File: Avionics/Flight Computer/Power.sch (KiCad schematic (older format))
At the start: 17 parts, among them U8 MAX17243

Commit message: Changed LED configuration, added smart driver chip to let all the CPUs access it..
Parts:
- C45, C47, R10, R11, R13: Voltage 50V -> 16V
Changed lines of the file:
@@
 BIAS
 $Comp
-L GND #PWR0119
+L GND #PWR0123
 U 1 1 58AB8EE1
 P 6050 4450
-F 0 "#PWR0119" H 2800 -350 50  0001 C CNN
+F 0 "#PWR0123" H 2800 -350 50  0001 C CNN
 F 1 "GND" H 6055 4277 50  0000 C CNN
 F 2 "" H 2800 -100 50  0001 C CNN
@@
 R11 sets oscillation frequency to 2.2MHz
 $Comp
-L +3.3V #PWR0120
+L +3.3V #PWR0124
 U 1 1 58AB9BA4
 P 8600 3100
-F 0 "#PWR0120" H 3600 0   50  0001 C CNN
+F 0 "#PWR0124" H 3600 0   50  0001 C CNN
 F 1 "+3.3V" H 8615 3273 50  0000 C CNN
 F 2 "" H 3600 150 50  0001 C CNN
@@
 PGOOD
 $Comp
-L GND #PWR0121
+L GND #PWR0125
 U 1 1 58ABCF35
 P 3500 3300
-F 0 "#PWR0121" H 250 -1500 50  0001 C CNN
+F 0 "#PWR0125" H 250 -1500 50  0001 C CNN
 F 1 "GND" H 3505 3127 50  0000 C CNN
 F 2 "" H 250 -1250 50  0001 C CNN
@@
 $EndComp
 $Comp
-L GND #PWR0122
+L GND #PWR0126
 U 1 1 58ABD05E
 P 2750 3300
-F 0 "#PWR0122" H -500 -1500 50  0001 C CNN
+F 0 "#PWR0126" H -500 -1500 50  0001 C CNN
 F 1 "GND" H 2755 3127 50  0000 C CNN
 F 2 "" H -500 -1250 50  0001 C CNN
@@
 Connection ~ 2750 2900
 $Comp
-L GND #PWR0123
+L GND #PWR0127
 U 1 1 58ABDCB9
 P 2000 3300
-F 0 "#PWR0123" H -1250 -1500 50  0001 C CNN
+F 0 "#PWR0127" H -1250 -1500 50  0001 C CNN
 F 1 "GND" H 2005 3127 50  0000 C CNN
 F 2 "" H -1250 -1250 50  0001 C CNN
@@
 Connection ~ 8250 3100
 $Comp
-L GND #PWR0124
+L GND #PWR0128
 U 1 1 58ABEDD8
 P 7850 3450
-F 0 "#PWR0124" H 4600 -1350 50  0001 C CNN
+F 0 "#PWR0128" H 4600 -1350 50  0001 C CNN
 F 1 "GND" H 7855 3277 50  0000 C CNN
 F 2 "" H 4600 -1100 50  0001 C CNN
@@
 $EndComp
 $Comp
-L GND #PWR0125
+L GND #PWR0129
 U 1 1 58ABEEB5
 P 8250 3450
-F 0 "#PWR0125" H 5000 -1350 50  0001 C CNN
+F 0 "#PWR0129" H 5000 -1350 50  0001 C CNN
 F 1 "GND" H 8255 3277 50  0000 C CNN
 F 2 "" H 5000 -1100 50  0001 C CNN
@@
 	850  2450 850  2350
 $Comp
-L +BATT #PWR0126
+L +BATT #PWR0130
 U 1 1 58B2E558
 P 850 2850
-F 0 "#PWR0126" H -200 -50 50  0001 C CNN
+F 0 "#PWR0130" H -200 -50 50  0001 C CNN
 F 1 "+BATT" H 865 3023 50  0000 C CNN
 F 2 "" H -200 100 50  0001 C CNN
@@
 $EndComp
 $Comp
-L VUSB #PWR0127
+L VUSB #PWR0131
 U 1 1 58B2E98C
 P 850 2350
-F 0 "#PWR0127" H -300 250 50  0001 C CNN
+F 0 "#PWR0131" H -300 250 50  0001 C CNN
 F 1 "VUSB" H 865 2523 50  0000 C CNN
 F 2 "" H -300 400 50  0001 C CNN
@@
 F 3 "" V -370 1100 50  0001 C CNN
 F 4 "1%" H 4220 3659 60  0000 L CNN "Tolerance"
-F 5 "50V" V -200 1100 60  0001 C CNN "Voltage"
+F 5 "16V" V -200 1100 60  0001 C CNN "Voltage"
 F 6 "0.062W" V -100 1100 60  0001 C CNN "Power"
 F 7 "Thin Film" V 0   1100 60  0001 C CNN "Material"
@@
 F 2 "Capacitors_SMD:C_0402" H 2288 -300 50  0001 C CNN
 F 3 "" H 2250 -150 50  0001 C CNN
-F 4 "50V" H 2350 -200 60  0001 L CNN "Voltage"
+F 4 "16V" H 2350 -200 60  0001 L CNN "Voltage"
 F 5 "20%" H 2350 -100 60  0001 L CNN "Tolerance"
 F 6 "X7R" H 2300 0   60  0001 L CNN "Type"
@@
 F 3 "" V 30  1450 50  0001 C CNN
 F 4 "1%" H 4620 4009 60  0000 L CNN "Tolerance"
-F 5 "50V" V 200 1450 60  0001 C CNN "Voltage"
+F 5 "16V" V 200 1450 60  0001 C CNN "Voltage"
 F 6 "0.062W" V 300 1450 60  0001 C CNN "Power"
 F 7 "Thin Film" V 400 1450 60  0001 C CNN "Material"
@@
 F 2 "Capacitors_SMD:C_0402" H 4888 -1050 50  0001 C CNN
 F 3 "" H 4850 -900 50  0001 C CNN
-F 4 "50V" H 4950 -950 60  0001 L CNN "Voltage"
+F 4 "16V" H 4950 -950 60  0001 L CNN "Voltage"
 F 5 "20%" H 4950 -850 60  0001 L CNN "Tolerance"
 F 6 "X7R" H 4900 -750 60  0001 L CNN "Type"
@@
 F 3 "" V 2930 750 50  0001 C CNN
 F 4 "1%" H 7520 3309 60  0000 L CNN "Tolerance"
-F 5 "50V" V 3100 750 60  0001 C CNN "Voltage"
+F 5 "16V" V 3100 750 60  0001 C CNN "Voltage"
 F 6 "0.062W" V 3200 750 60  0001 C CNN "Power"
 F 7 "Thin Film" V 3300 750 60  0001 C CNN "Material"
@@
 $EndComp
 $Comp
-L PWR_FLAG #FLG0128
+L PWR_FLAG #FLG0132
 U 1 1 58BE5ADD
 P 8150 3100
-F 0 "#FLG0128" H 8200 3150 50  0001 C CNN
+F 0 "#FLG0132" H 8200 3150 50  0001 C CNN
 F 1 "PWR_FLAG" H 8150 3274 50  0000 C CNN
 F 2 "" H -1500 550 50  0001 C CNN
@@
 Connection ~ 8150 3100
 $Comp
-L PWR_FLAG #FLG0129
+L PWR_FLAG #FLG0133
 U 1 1 58BE6F80
 P 4300 2900
-F 0 "#FLG0129" H 0   925 50  0001 C CNN
+F 0 "#FLG0133" H 0   925 50  0001 C CNN
 F 1 "PWR_FLAG" H 4300 3074 50  0000 C CNN
 F 2 "" H 0   850 50  0001 C CNN

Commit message: DFM/BOM Optimizations
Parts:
- R10: value 20k -> 18k
- R11: value 12k -> 15k
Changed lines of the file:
@@
 P 4150 3750
 F 0 "R10" H 4220 3849 50  0000 L CNN
-F 1 "20k" H 4220 3758 50  0000 L CNN
+F 1 "18k" H 4220 3758 50  0000 L CNN
 F 2 "Resistors_SMD:R_0402" V -650 1100 50  0001 C CNN
 F 3 "" V -370 1100 50  0001 C CNN
@@
 P 4550 4100
 F 0 "R11" H 4620 4199 50  0000 L CNN
-F 1 "12k" H 4620 4108 50  0000 L CNN
+F 1 "15k" H 4620 4108 50  0000 L CNN
 F 2 "Resistors_SMD:R_0402" V -250 1450 50  0001 C CNN
 F 3 "" V 30  1450 50  0001 C CNN

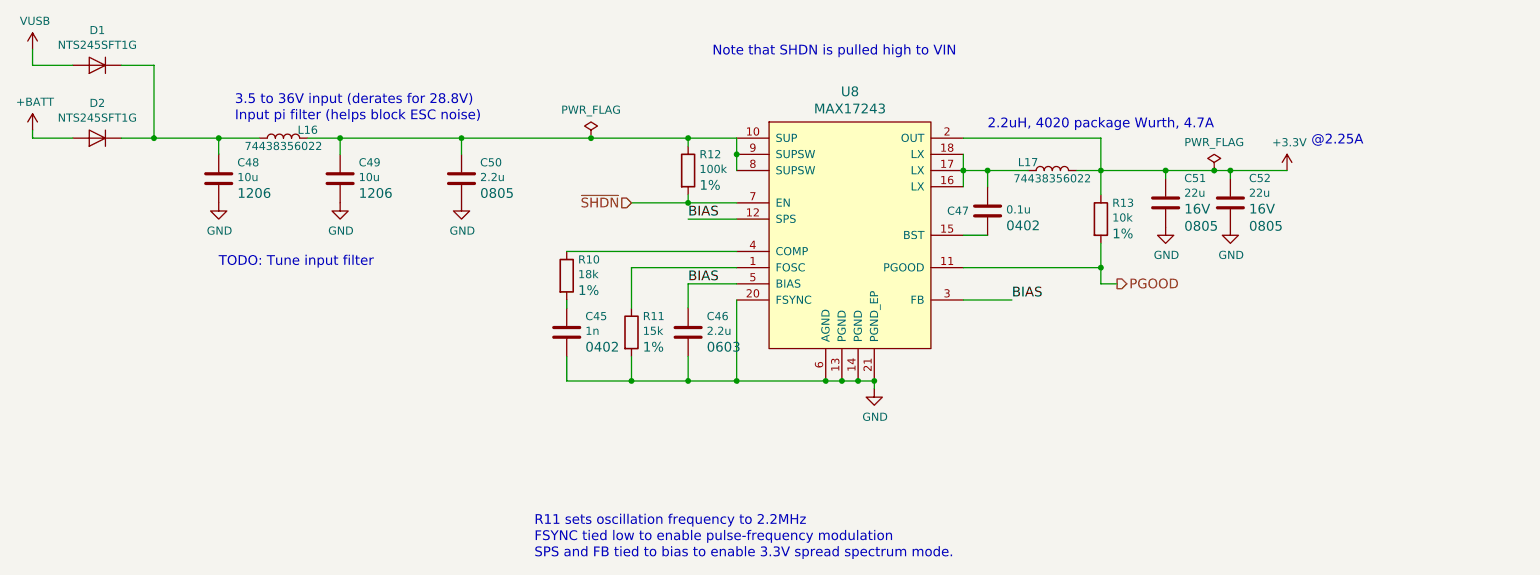
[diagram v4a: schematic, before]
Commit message: Built outputs and added manufacturing part numbers to make BOM search easier.
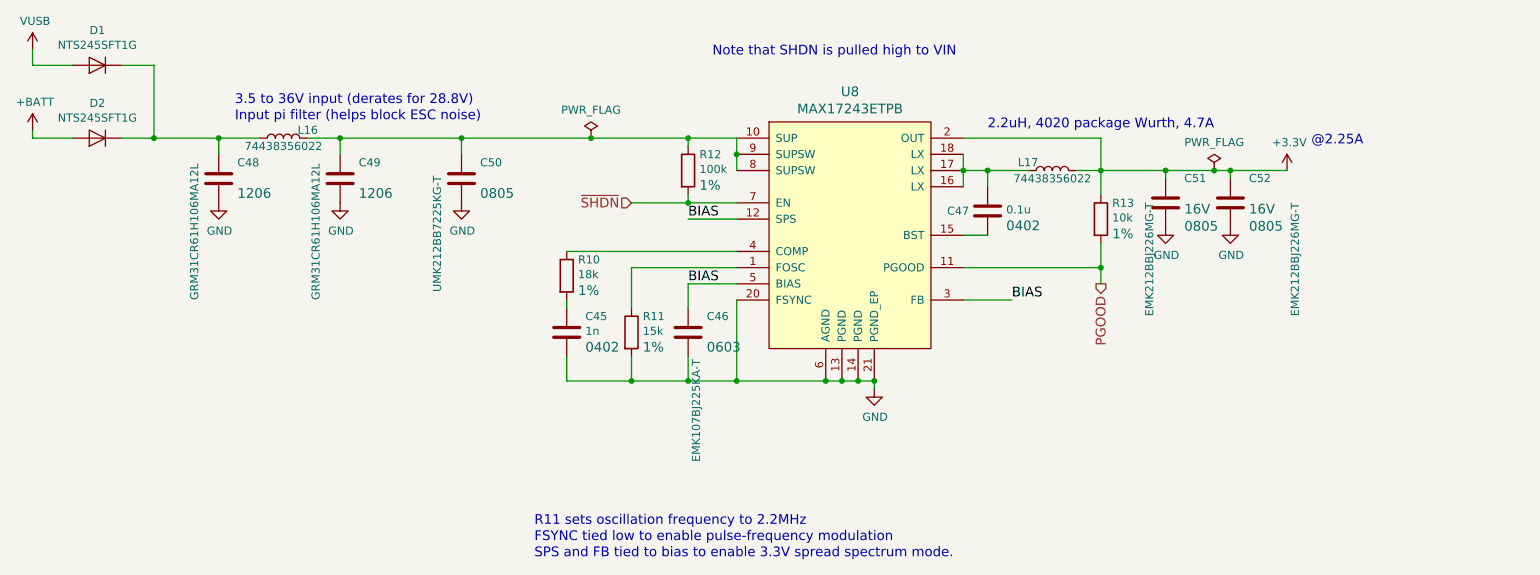
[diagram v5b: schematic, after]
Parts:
- C46: value 2.2u -> EMK107BJ225KA-T
- C48, C49: value 10u -> GRM31CR61H106MA12L
- C50: value 2.2u -> UMK212BB7225KG-T
- C51, C52: value 22u -> EMK212BBJ226MG-T
- U8: value MAX17243 -> MAX17243ETPB
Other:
- note removed: "TODO: Tune input filter"
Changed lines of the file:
@@
 BIAS
 $Comp
-L GND #PWR114
+L GND #PWR0123
 U 1 1 58AB8EE1
 P 6050 4450
-F 0 "#PWR114" H 2800 -350 50  0001 C CNN
+F 0 "#PWR0123" H 2800 -350 50  0001 C CNN
 F 1 "GND" H 6055 4277 50  0000 C CNN
 F 2 "" H 2800 -100 50  0001 C CNN
@@
 R11 sets oscillation frequency to 2.2MHz
 $Comp
-L +3.3V #PWR117
+L +3.3V #PWR0124
 U 1 1 58AB9BA4
 P 8600 3100
-F 0 "#PWR117" H 3600 0   50  0001 C CNN
+F 0 "#PWR0124" H 3600 0   50  0001 C CNN
 F 1 "+3.3V" H 8615 3273 50  0000 C CNN
 F 2 "" H 3600 150 50  0001 C CNN
@@
 Text HLabel 4550 3300 0    60   Input ~ 0
 ~SHDN
-Text HLabel 7550 3800 2    60   Output ~ 0
+Text HLabel 7450 3800 3    60   Output ~ 0
 PGOOD
 $Comp
-L GND #PWR113
+L GND #PWR0125
 U 1 1 58ABCF35
 P 3500 3300
-F 0 "#PWR113" H 250 -1500 50  0001 C CNN
+F 0 "#PWR0125" H 250 -1500 50  0001 C CNN
 F 1 "GND" H 3505 3127 50  0000 C CNN
 F 2 "" H 250 -1250 50  0001 C CNN
@@
 $EndComp
 $Comp
-L GND #PWR112
+L GND #PWR0126
 U 1 1 58ABD05E
 P 2750 3300
-F 0 "#PWR112" H -500 -1500 50  0001 C CNN
+F 0 "#PWR0126" H -500 -1500 50  0001 C CNN
 F 1 "GND" H 2755 3127 50  0000 C CNN
 F 2 "" H -500 -1250 50  0001 C CNN
@@
 Connection ~ 2750 2900
 $Comp
-L GND #PWR111
+L GND #PWR0127
 U 1 1 58ABDCB9
 P 2000 3300
-F 0 "#PWR111" H -1250 -1500 50  0001 C CNN
+F 0 "#PWR0127" H -1250 -1500 50  0001 C CNN
 F 1 "GND" H 2005 3127 50  0000 C CNN
 F 2 "" H -1250 -1250 50  0001 C CNN
@@
 Connection ~ 8250 3100
 $Comp
-L GND #PWR115
+L GND #PWR0128
 U 1 1 58ABEDD8
 P 7850 3450
-F 0 "#PWR115" H 4600 -1350 50  0001 C CNN
+F 0 "#PWR0128" H 4600 -1350 50  0001 C CNN
 F 1 "GND" H 7855 3277 50  0000 C CNN
 F 2 "" H 4600 -1100 50  0001 C CNN
@@
 $EndComp
 $Comp
-L GND #PWR116
+L GND #PWR0129
 U 1 1 58ABEEB5
 P 8250 3450
-F 0 "#PWR116" H 5000 -1350 50  0001 C CNN
+F 0 "#PWR0129" H 5000 -1350 50  0001 C CNN
 F 1 "GND" H 8255 3277 50  0000 C CNN
 F 2 "" H 5000 -1100 50  0001 C CNN
@@
 	0    -1   -1   0
 $EndComp
-Text Notes 2000 3700 0    60   ~ 0
-TODO: Tune input filter
-Wire Wire Line
-	7450 3800 7550 3800
 Wire Wire Line
 	7450 3700 6600 3700
@@
 	850  2450 850  2350
 $Comp
-L +BATT #PWR110
+L +BATT #PWR0130
 U 1 1 58B2E558
 P 850 2850
-F 0 "#PWR110" H -200 -50 50  0001 C CNN
+F 0 "#PWR0130" H -200 -50 50  0001 C CNN
 F 1 "+BATT" H 865 3023 50  0000 C CNN
 F 2 "" H -200 100 50  0001 C CNN
@@
 $EndComp
 $Comp
-L VUSB #PWR109
+L VUSB #PWR0131
 U 1 1 58B2E98C
 P 850 2350
-F 0 "#PWR109" H -300 250 50  0001 C CNN
+F 0 "#PWR0131" H -300 250 50  0001 C CNN
 F 1 "VUSB" H 865 2523 50  0000 C CNN
 F 2 "" H -300 400 50  0001 C CNN
@@
 P 2000 3150
 F 0 "C48" H 2115 3249 50  0000 L CNN
-F 1 "10u" H 2115 3158 50  0000 L CNN
+F 1 "GRM31CR61H106MA12L" V 1850 2400 50  0000 L CNN
 F 2 "Capacitors_SMD:C_1206" H 138 -1250 50  0001 C CNN
 F 3 "" H 100 -1100 50  0001 C CNN
@@
 P 2750 3150
 F 0 "C49" H 2865 3249 50  0000 L CNN
-F 1 "10u" H 2865 3158 50  0000 L CNN
+F 1 "GRM31CR61H106MA12L" V 2600 2400 50  0000 L CNN
 F 2 "Capacitors_SMD:C_1206" H 888 -1250 50  0001 C CNN
 F 3 "" H 850 -1100 50  0001 C CNN
@@
 P 3500 3150
 F 0 "C50" H 3615 3249 50  0000 L CNN
-F 1 "2.2u" H 3615 3158 50  0000 L CNN
+F 1 "UMK212BB7225KG-T" V 3350 2450 50  0000 L CNN
 F 2 "Capacitors_SMD:C_0805" H 1638 -1250 50  0001 C CNN
 F 3 "" H 1600 -1100 50  0001 C CNN
@@
 P 4900 4100
 F 0 "C46" H 5015 4199 50  0000 L CNN
-F 1 "2.2u" H 5015 4108 50  0000 L CNN
+F 1 "EMK107BJ225KA-T" V 4950 3300 50  0000 L CNN
 F 2 "Capacitors_SMD:C_0603" H 3038 -300 50  0001 C CNN
 F 3 "" H 3000 -150 50  0001 C CNN
@@
 P 7850 3300
 F 0 "C51" H 7965 3452 50  0000 L CNN
-F 1 "22u" H 7965 3361 50  0000 L CNN
+F 1 "EMK212BBJ226MG-T" V 7750 2600 50  0000 L CNN
 F 2 "Capacitors_SMD:C_0805" H 5988 -1100 50  0001 C CNN
 F 3 "" H 5950 -950 50  0001 C CNN
@@
 P 8250 3300
 F 0 "C52" H 8365 3452 50  0000 L CNN
-F 1 "22u" H 8365 3361 50  0000 L CNN
+F 1 "EMK212BBJ226MG-T" V 8650 2600 50  0000 L CNN
 F 2 "Capacitors_SMD:C_0805" H 6388 -1100 50  0001 C CNN
 F 3 "" H 6350 -950 50  0001 C CNN
@@
 $EndComp
 $Comp
-L PWR_FLAG #FLG16
+L PWR_FLAG #FLG0132
 U 1 1 58BE5ADD
 P 8150 3100
-F 0 "#FLG16" H 8200 3150 50  0001 C CNN
+F 0 "#FLG0132" H 8200 3150 50  0001 C CNN
 F 1 "PWR_FLAG" H 8150 3274 50  0000 C CNN
 F 2 "" H -1500 550 50  0001 C CNN
@@
 Connection ~ 8150 3100
 $Comp
-L PWR_FLAG #FLG15
+L PWR_FLAG #FLG0133
 U 1 1 58BE6F80
 P 4300 2900
-F 0 "#FLG15" H 0   925 50  0001 C CNN
+F 0 "#FLG0133" H 0   925 50  0001 C CNN
 F 1 "PWR_FLAG" H 4300 3074 50  0000 C CNN
 F 2 "" H 0   850 50  0001 C CNN
@@
 P 5900 3500
 F 0 "U8" H 5900 4387 60  0000 C CNN
-F 1 "MAX17243" H 5900 4281 60  0000 C CNN
+F 1 "MAX17243ETPB" H 5900 4281 60  0000 C CNN
 F 2 "Housings_DFN_QFN:QFN-20-1EP_5x5mm_Pitch0.65mm" H -2550 2100 60  0001 C CNN
 F 3 "http://datasheets.maximintegrated.com/en/ds/MAX17242-MAX17243.pdf" H -2550 0   60  0001 C CNN

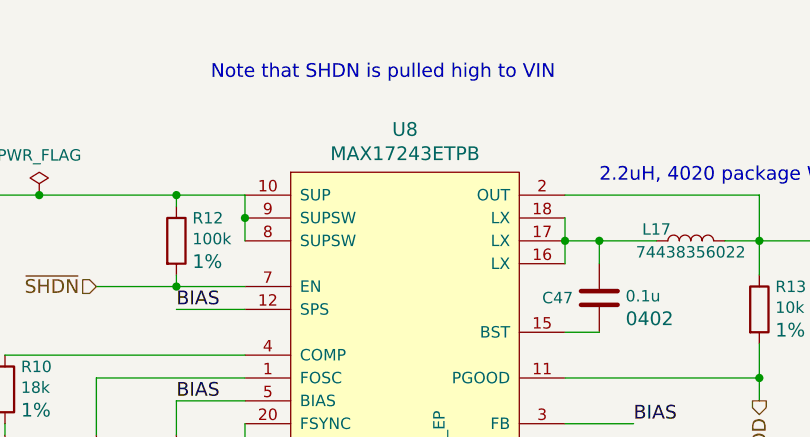
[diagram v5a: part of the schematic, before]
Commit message: Updated more manufacturing part numbers for macrofab compatibility.
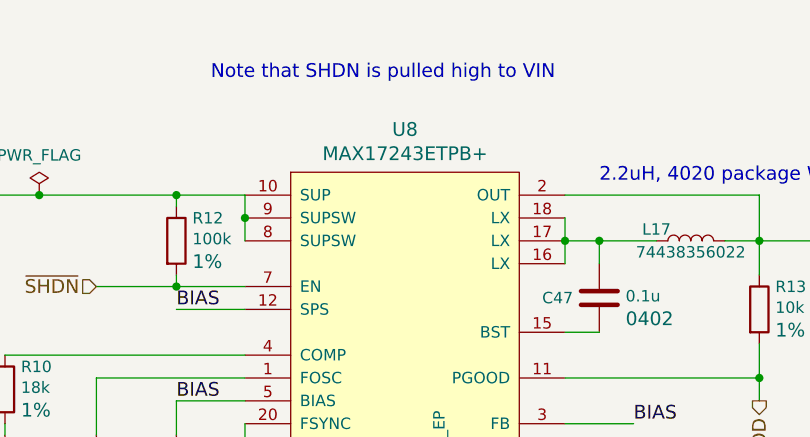
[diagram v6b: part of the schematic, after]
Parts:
- U8: value MAX17243ETPB -> MAX17243ETPB+
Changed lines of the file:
@@
 P 5900 3500
 F 0 "U8" H 5900 4387 60  0000 C CNN
-F 1 "MAX17243ETPB" H 5900 4281 60  0000 C CNN
+F 1 "MAX17243ETPB+" H 5900 4281 60  0000 C CNN
 F 2 "Housings_DFN_QFN:QFN-20-1EP_5x5mm_Pitch0.65mm" H -2550 2100 60  0001 C CNN
 F 3 "http://datasheets.maximintegrated.com/en/ds/MAX17242-MAX17243.pdf" H -2550 0   60  0001 C CNN

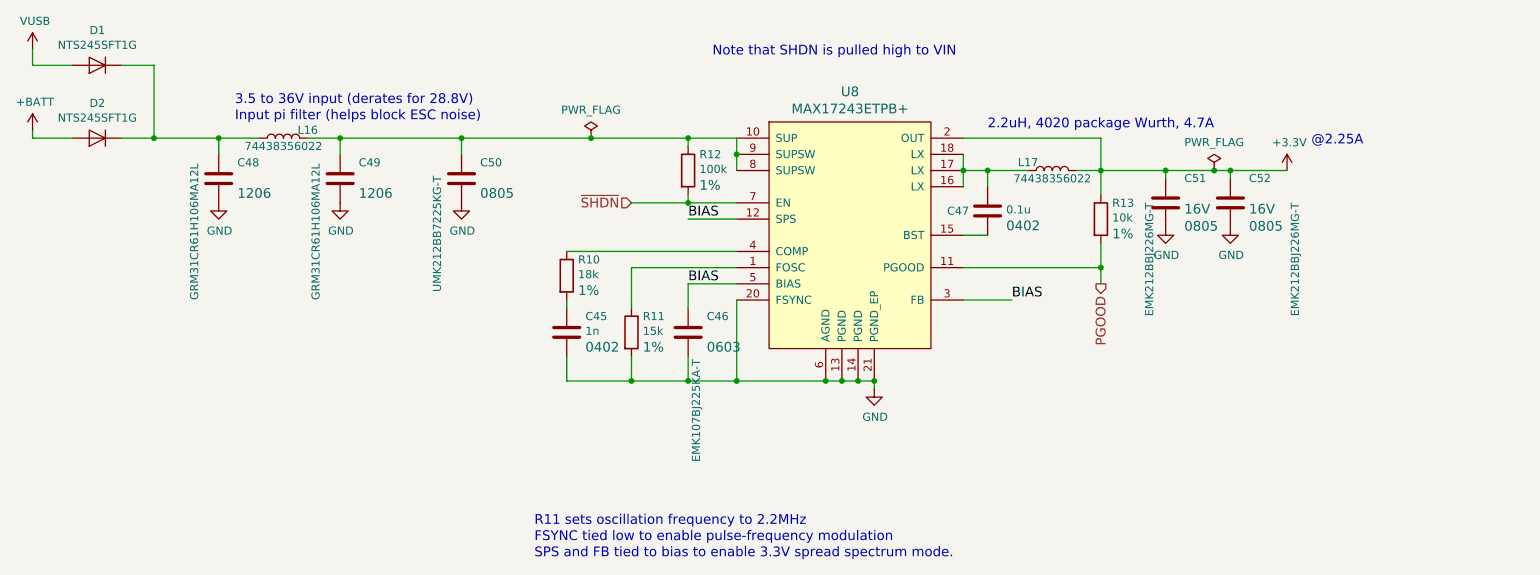
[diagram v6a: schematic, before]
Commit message: Finished rerouting and power supply update. Replaced connectors and did initial replacement.
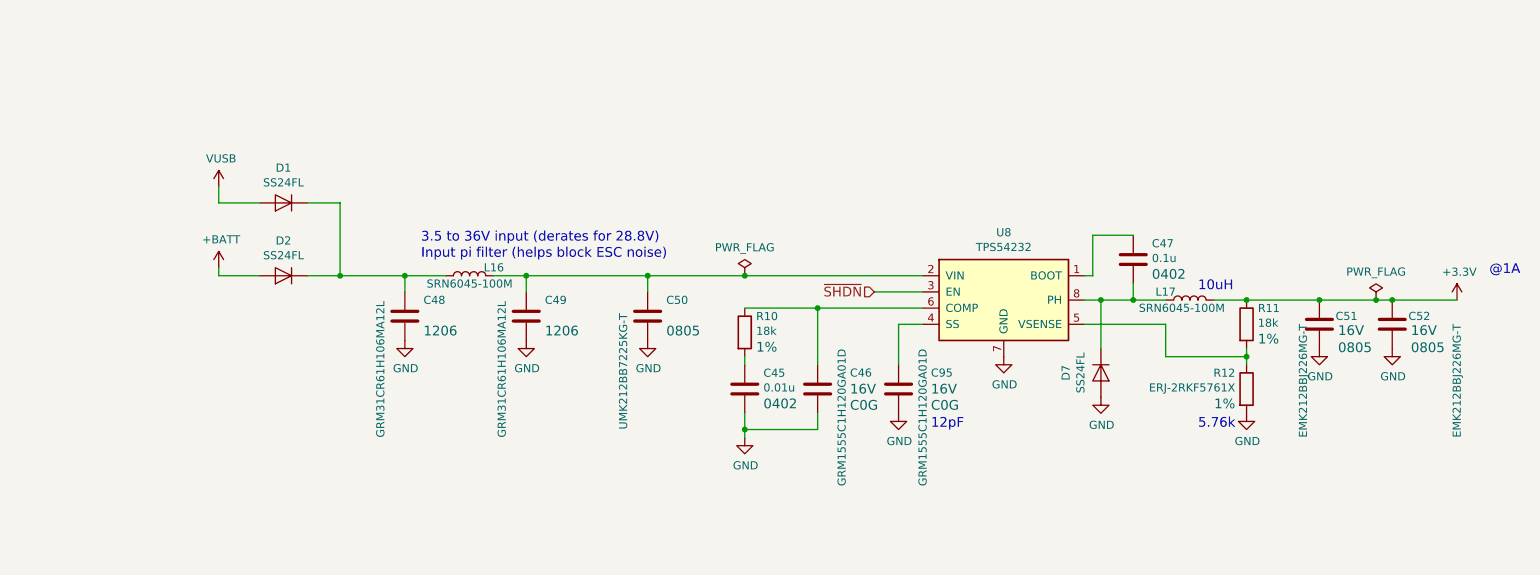
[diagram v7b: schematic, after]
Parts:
- removed R13: 10k, Resistors_SMD:R_0402, symbol R
- removed U8: MAX17243ETPB+, Housings_DFN_QFN:QFN-20-1EP_5x5mm_Pitch0.65mm, symbol MAX17243
- added C95: GRM1555C1H120GA01D, Capacitors_SMD:C_0402, symbol C
- added D7: SS24FL, Diodes_SMD:D_SOD-123F, symbol D
- added U8: TPS54232, Housings_SOIC:SOIC-8_3.9x4.9mm_Pitch1.27mm, symbol TPS54232
- C45: value 1n -> 0.01u
- C46: value EMK107BJ225KA-T -> GRM1555C1H120GA01D; footprint Capacitors_SMD:C_0603 -> Capacitors_SMD:C_0402; Package 0603 -> 0402; Type X7R -> C0G
- D1, D2: value NTS245SFT1G -> SS24FL
- L16, L17: value 74438356022 -> SRN6045-100M; footprint Inductors_SMD:L_Wuerth_MAPI-4020 -> Inductors_SMD:L_BOURNS-SRN6045
- R11: value 15k -> 18k
- R12: value 100k -> ERJ-2RKF5761X; Voltage 50V -> 16V
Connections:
- net BIAS is gone; now on net GND: C46.1
- net +3V3: now also R11.1
- net GND: now also R12.2, C95.1, D7.2 (A), U8.7 (GND); no longer C46.2, R11.2
- net ~SHDN: now also U8.3 (EN); no longer R12.2
- net at C49.1, C50.1, L16.2: now also U8.2 (VIN); no longer R12.1
- net at C47.1, L17.2: now also D7.1 (K), U8.8 (PH)
- net at R10.1: now also C46.2, U8.6 (COMP)
- net at C47.2: now also U8.1 (BOOT)
- new net: C95.2, U8.4 (SS)
- new net: R11.2, R12.1, U8.5 (VSENSE)
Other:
- note added: "10uH"
- note added: "12pF"
- note added: "5.76k"
- note added: "@1A"
- note removed: "2.2uH, 4020 package Wurth, 4.7A"
- note removed: "@2.25A"
- note removed: "FSYNC tied low to enable pulse-frequency modulation"
- note removed: "Note that SHDN is pulled high to VIN"
- note removed: "R11 sets oscillation frequency to 2.2MHz"
- note removed: "SPS and FB tied to bias to enable 3.3V spread spectrum mode."
- moved on the sheet: C45, C47, C48, C49, C50, C51, C52, D1, D2, L16, R10
